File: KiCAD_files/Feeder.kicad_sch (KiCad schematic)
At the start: 82 parts, among them J405 Conn_01x02_Male, J406 Conn_01x02_Male, J501 Conn_01x03, Q501 60V N channel, Q502 TK13P25D,RQ, T501 PA2467NL, U407 OPA316, U501 NCP12700, U503 TL431MFDT,215

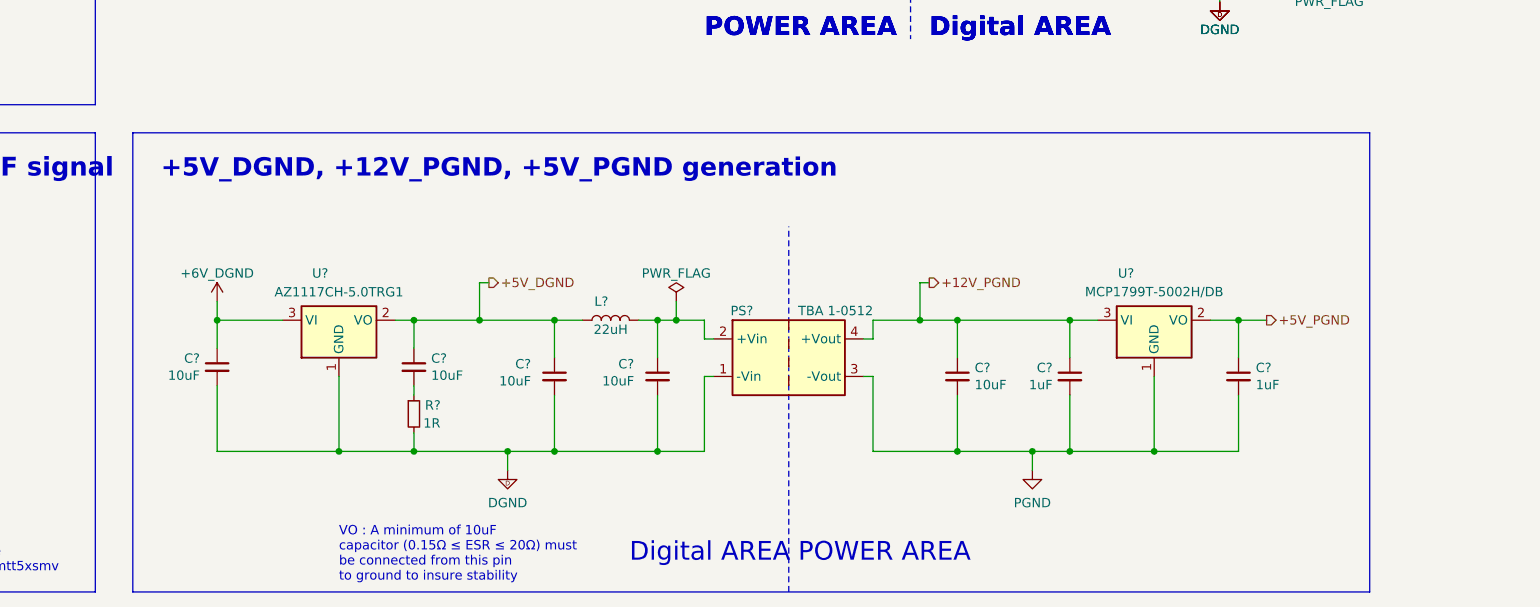
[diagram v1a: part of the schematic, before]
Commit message: added MCP1799T-5002H/DB in sch, forgot in previous commit
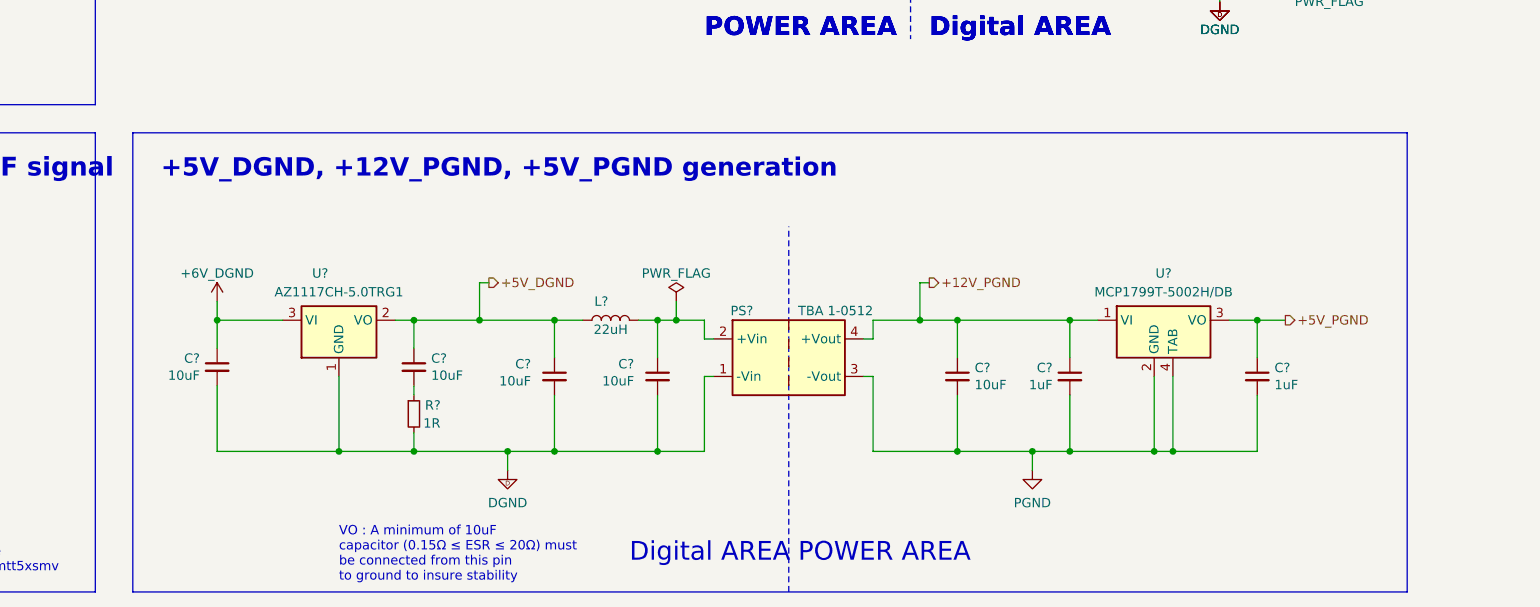
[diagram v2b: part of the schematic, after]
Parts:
- removed U?: MCP1799T-5002H/DB, Package_TO_SOT_SMD:SOT-223, symbol Regulator_Linear:MCP1754S-5002xCB
- added U?: MCP1799T-5002H/DB, Package_TO_SOT_SMD:SOT-223, symbol Symbols:MCP1799T-5002H/DB
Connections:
- net +12V_PGND: now also U?.1 (VI)
- net +5V_PGND: now also U?.3 (VO)
- net PGND: now also U?.2 (GND), U?.4 (TAB)
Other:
- moved on the sheet: C?
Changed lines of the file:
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@@
   (junction (at 154.94 127) (diameter 0) (color 0 0 0 0)
   )
-  (junction (at 264.16 261.62) (diameter 0) (color 0 0 0 0)
+  (junction (at 266.7 261.62) (diameter 0) (color 0 0 0 0)
   )
   (junction (at 49.53 96.52) (diameter 0) (color 0 0 0 0)
@@
   (junction (at 247.65 261.62) (diameter 0) (color 0 0 0 0)
   )
+  (junction (at 264.16 261.62) (diameter 0) (color 0 0 0 0)
+  )
   (junction (at 182.88 261.62) (diameter 0) (color 0 0 0 0)
   )
@@
   (junction (at 153.67 261.62) (diameter 0) (color 0 0 0 0)
   )
-  (junction (at 275.59 243.84) (diameter 0) (color 0 0 0 0)
-  )
   (junction (at 196.85 243.84) (diameter 0) (color 0 0 0 0)
   )
@@
   (junction (at 181.61 104.14) (diameter 0) (color 0 0 0 0)
   )
+  (junction (at 278.13 243.84) (diameter 0) (color 0 0 0 0)
+  )
   (junction (at 285.75 185.42) (diameter 0) (color 0 0 0 0)
   )
@@
   (junction (at 273.05 176.53) (diameter 0) (color 0 0 0 0)
   )
+  (wire (pts (xy 266.7 261.62) (xy 278.13 261.62))
+    (stroke (width 0.5) (type default))
+  )
   (wire (pts (xy 38.1 261.62) (xy 38.1 267.97))
     (stroke (width 0) (type default))
@@
     (stroke (width 0.5) (type default))
   )
+  (wire (pts (xy 264.16 251.46) (xy 264.16 261.62))
+    (stroke (width 0.5) (type default))
+  )
   (wire (pts (xy 64.77 187.96) (xy 64.77 189.23))
     (stroke (width 0) (type default))
@@
     (stroke (width 0) (type default))
   )
-  (wire (pts (xy 271.78 243.84) (xy 275.59 243.84))
-    (stroke (width 0.5) (type default))
-  )
   (wire (pts (xy 165.1 147.32) (xy 165.1 153.67))
     (stroke (width 0) (type default))
@@
     (stroke (width 0) (type default))
   )
-  (wire (pts (xy 275.59 254) (xy 275.59 261.62))
+  (wire (pts (xy 278.13 254) (xy 278.13 261.62))
     (stroke (width 0.5) (type default))
   )
@@
     (stroke (width 0.5) (type default))
   )
-  (wire (pts (xy 275.59 248.92) (xy 275.59 243.84))
+  (wire (pts (xy 278.13 248.92) (xy 278.13 243.84))
     (stroke (width 0.5) (type default))
   )
@@
     (stroke (width 0) (type default))
   )
+  (wire (pts (xy 266.7 251.46) (xy 266.7 261.62))
+    (stroke (width 0.5) (type default))
+  )
   (wire (pts (xy 205.74 104.14) (xy 219.71 104.14))
     (stroke (width 0) (type default))
   )
-  (wire (pts (xy 264.16 251.46) (xy 264.16 261.62))
-    (stroke (width 0.5) (type default))
-  )
   (wire (pts (xy 327.66 106.68) (xy 327.66 109.22))
     (stroke (width 0.5) (type default))
@@
     (stroke (width 0) (type default))
   )
-  (wire (pts (xy 275.59 261.62) (xy 264.16 261.62))
-    (stroke (width 0.5) (type default))
-  )
   (wire (pts (xy 247.65 261.62) (xy 252.73 261.62))
     (stroke (width 0.5) (type default))
@@
     (stroke (width 0.5) (type default))
   )
+  (wire (pts (xy 274.32 243.84) (xy 278.13 243.84))
+    (stroke (width 0.5) (type default))
+  )
   (wire (pts (xy 181.61 104.14) (xy 181.61 101.6))
     (stroke (width 0) (type default))
@@
     (stroke (width 0.5) (type default))
   )
-  (wire (pts (xy 275.59 243.84) (xy 279.4 243.84))
+  (wire (pts (xy 278.13 243.84) (xy 281.94 243.84))
     (stroke (width 0.5) (type default))
   )
@@
     (stroke (width 0) (type default))
   )
+  (wire (pts (xy 264.16 261.62) (xy 266.7 261.62))
+    (stroke (width 0.5) (type default))
+  )
   (wire (pts (xy 285.75 90.17) (xy 285.75 118.11))
     (stroke (width 0) (type default))
@@
     (fill (type none))
   )
-  (rectangle (start 125.73 218.44) (end 293.37 280.67)
+  (rectangle (start 125.73 218.44) (end 298.45 280.67)
     (stroke (width 0) (type default))
     (fill (type none))
@@
     (effects (font (size 1.27 1.27)) (justify left))
   )
-  (hierarchical_label "+5V_PGND" (shape output) (at 279.4 243.84 0) (fields_autoplaced)
+  (hierarchical_label "+5V_PGND" (shape output) (at 281.94 243.84 0) (fields_autoplaced)
     (effects (font (size 1.27 1.27)) (justify left))
   )
@@
     )
   )
+  (symbol (lib_id "Symbols:MCP1799T-5002H/DB") (at 264.16 243.84 0) (unit 1)
+    (in_bom yes) (on_board yes) (dnp no) (fields_autoplaced)
+    (property "Reference" "U?" (at 265.43 237.49 0)
+      (effects (font (size 1.27 1.27)))
+    )
+    (property "Value" "MCP1799T-5002H/DB" (at 265.43 240.03 0)
+      (effects (font (size 1.27 1.27)))
+    )
+    (property "Footprint" "Package_TO_SOT_SMD:SOT-223" (at 264.16 238.125 0)
+      (effects (font (size 1.27 1.27)) hide)
+    )
+    (property "Datasheet" "https://www.mouser.fr/datasheet/2/268/MCP1799_Data_Sheet_20006248B-2887414.pdf" (at 265.43 232.41 0)
+      (effects (font (size 1.27 1.27)) hide)
+    )
+    (property "manf#" "MCP1799T-5002H/DB" (at 264.16 243.84 0)
+      (effects (font (size 1.27 1.27)) hide)
+    )
+    (pin "1")
+    (pin "2")
+    (pin "3")
+    (pin "4")
+    (instances
+      (project "ownverter"
+        (path "/8d0c1d66-35ef-4a53-a28f-436a11b54f42/bce1534c-362e-45ed-a9dd-a44d6954485a"
+          (reference "U?") (unit 1)
+        )
+      )
+    )
+  )
   (symbol (lib_id "Device:R_Small") (at 38.1 259.08 180) (unit 1)
     (in_bom yes) (on_board yes) (dnp no)
@@
     )
   )
-  (symbol (lib_id "Regulator_Linear:MCP1754S-5002xCB") (at 264.16 243.84 0) (unit 1)
-    (in_bom yes) (on_board yes) (dnp no)
-    (property "Reference" "U?" (at 260.35 237.49 0)
-      (effects (font (size 1.27 1.27)))
-    )
-    (property "Value" "MCP1799T-5002H/DB" (at 264.16 240.0046 0)
-      (effects (font (size 1.27 1.27)))
-    )
-    (property "Footprint" "Package_TO_SOT_SMD:SOT-223" (at 264.16 238.125 0)
-      (effects (font (size 1.27 1.27)) hide)
-    )
-    (property "Datasheet" "https://www.mouser.fr/datasheet/2/268/MCP1799_Data_Sheet_20006248B-2887414.pdf" (at 264.16 243.84 0)
-      (effects (font (size 1.27 1.27)) hide)
-    )
-    (property "DNP" "x" (at 264.16 243.84 0)
-      (effects (font (size 1.27 1.27)) hide)
-    )
-    (property "manf#" "MCP1799T-5002H/DB" (at 264.16 243.84 0)
-      (effects (font (size 1.27 1.27)) hide)
-    )
-    (pin "1")
-    (pin "2")
-    (pin "3")
-    (instances
-      (project "ownverter"
-        (path "/8d0c1d66-35ef-4a53-a28f-436a11b54f42/122c01f4-f23e-4db0-9503-7261d96dc78b"
-          (reference "U?") (unit 1)
-        )
-        (path "/8d0c1d66-35ef-4a53-a28f-436a11b54f42"
-          (reference "U?") (unit 1)
-        )
-        (path "/8d0c1d66-35ef-4a53-a28f-436a11b54f42/bce1534c-362e-45ed-a9dd-a44d6954485a"
-          (reference "U505") (unit 1)
-        )
-      )
-    )
-  )
   (symbol (lib_id "Device:L") (at 43.18 46.99 90) (unit 1)
     (in_bom yes) (on_board yes) (dnp no) (fields_autoplaced)
@@
     )
   )
-  (symbol (lib_id "Device:C_Small") (at 275.59 251.46 0) (unit 1)
+  (symbol (lib_id "Device:C_Small") (at 278.13 251.46 0) (unit 1)
     (in_bom yes) (on_board yes) (dnp no)
-    (property "Reference" "C?" (at 277.9268 250.2916 0)
+    (property "Reference" "C?" (at 280.4668 250.2916 0)
       (effects (font (size 1.27 1.27)) (justify left))
     )
-    (property "Value" "1uF" (at 277.9268 252.603 0)
+    (property "Value" "1uF" (at 280.4668 252.603 0)
       (effects (font (size 1.27 1.27)) (justify left))
     )
-    (property "Footprint" "Footprints:C_0805_2012Metric" (at 275.59 251.46 0)
+    (property "Footprint" "Footprints:C_0805_2012Metric" (at 278.13 251.46 0)
       (effects (font (size 1.27 1.27)) hide)
     )
-    (property "Datasheet" "~" (at 275.59 251.46 0)
+    (property "Datasheet" "~" (at 278.13 251.46 0)
       (effects (font (size 1.27 1.27)) hide)
     )
-    (property "DNP" "x" (at 275.59 251.46 0)
+    (property "DNP" "x" (at 278.13 251.46 0)
       (effects (font (size 1.27 1.27)) hide)
     )
-    (property "manf#" "UMK212B7105KGHT " (at 275.59 251.46 0)
+    (property "manf#" "UMK212B7105KGHT " (at 278.13 251.46 0)
       (effects (font (size 1.27 1.27)) hide)
     )

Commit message: ready to import netlist
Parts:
- gave numbers to parts that had none: 1
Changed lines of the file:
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@@
   (symbol (lib_id "Symbols:MCP1799T-5002H/DB") (at 264.16 243.84 0) (unit 1)
     (in_bom yes) (on_board yes) (dnp no) (fields_autoplaced)
-    (property "Reference" "U?" (at 265.43 237.49 0)
+    (property "Reference" "U505" (at 265.43 237.49 0)
       (effects (font (size 1.27 1.27)))
     )
@@
       (project "ownverter"
         (path "/8d0c1d66-35ef-4a53-a28f-436a11b54f42/bce1534c-362e-45ed-a9dd-a44d6954485a"
-          (reference "U?") (unit 1)
+          (reference "U505") (unit 1)
         )
       )

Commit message: WIP PCB
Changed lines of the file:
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@@
     (stroke (width 0.5) (type default))
   )
-  (polyline (pts (xy 231.14 15.24) (xy 231.14 205.74))
+  (polyline (pts (xy 231.14 15.24) (xy 231.14 218.44))
     (stroke (width 0.15) (type dash))
   )

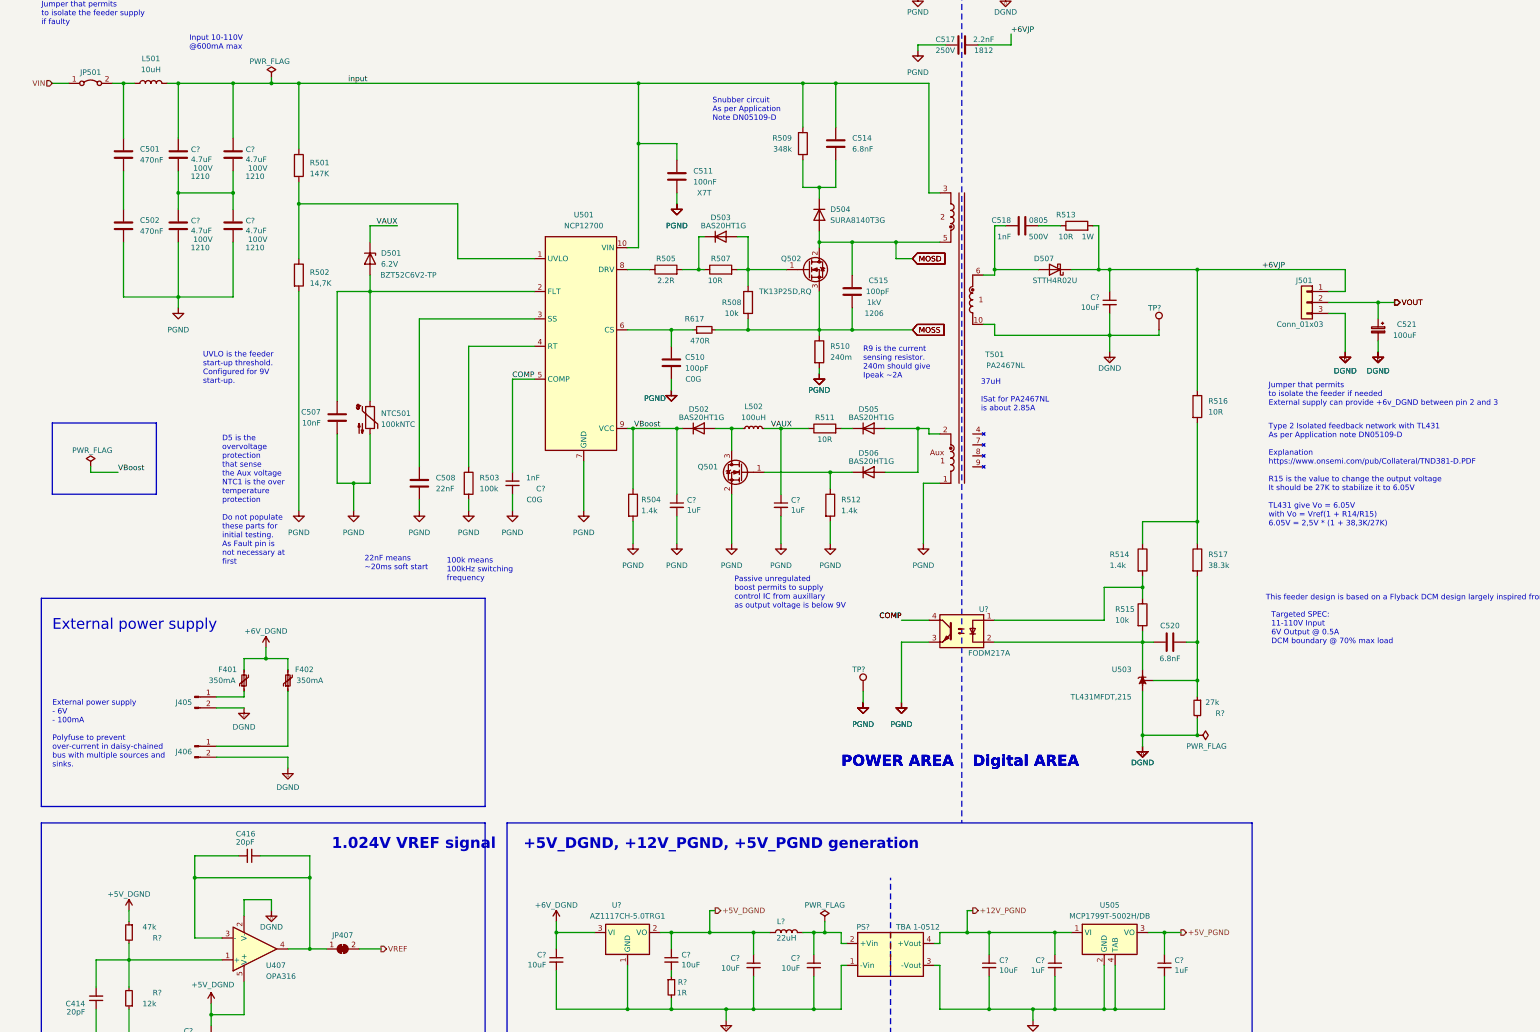
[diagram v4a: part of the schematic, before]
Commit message: changed schematic net labels for better comprehension
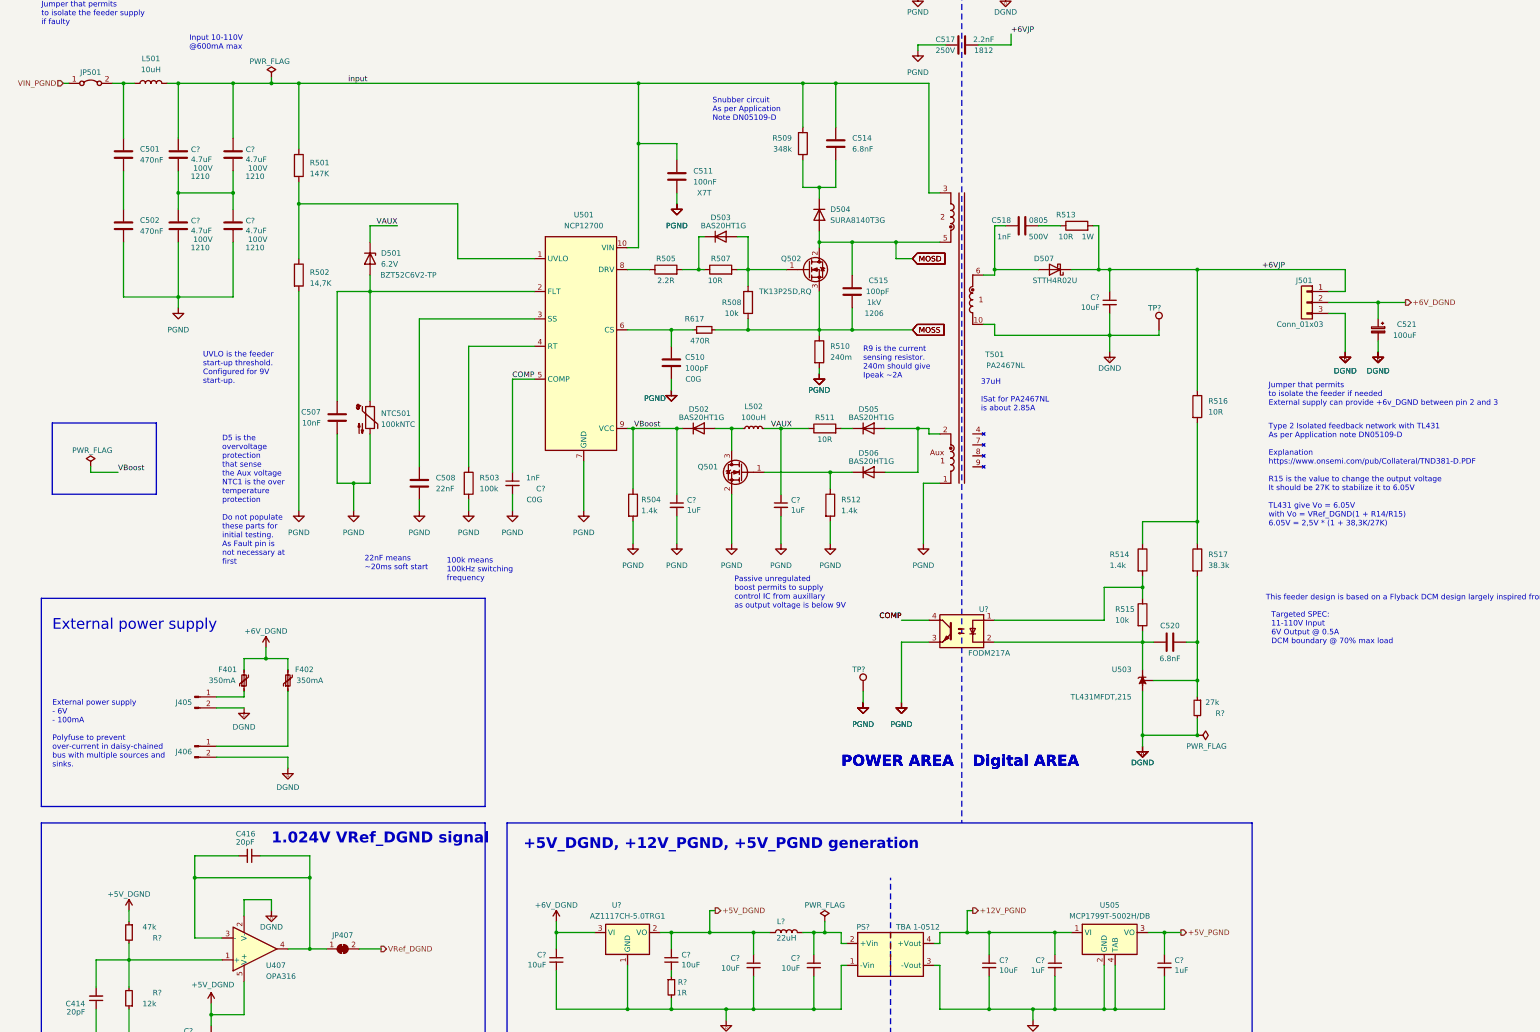
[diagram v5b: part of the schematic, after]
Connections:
- net VIN renamed VIN_PGND
- net VOUT renamed +6V_DGND
- net VREF renamed VRef_DGND
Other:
- note added: "1.024V VRef_DGND signal"
- note added: "Type 2 Isolated feedback network with TL431 As per Application note DN05109-D Explanation https://www.onsemi.com/pub/Collateral/TND381-D.PDF R15 is the value to change the output voltage It should be 27K to stabilize it to 6.05V TL431 give Vo = 6.05V with Vo = VRef_DGND(1 + R14/R15) 6.05V = 2,5V * (1 + 38,3K/27K)"
- note removed: "1.024V VREF signal"
- note removed: "Type 2 Isolated feedback network with TL431 As per Application note DN05109-D Explanation https://www.onsemi.com/pub/Collateral/TND381-D.PDF R15 is the value to change the output voltage It should be 27K to stabilize it to 6.05V TL431 give Vo = 6.05V with Vo = Vref(1 + R14/R15) 6.05V = 2,5V * (1 + 38,3K/27K)"
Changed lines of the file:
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@@
     (stroke (width 0) (type default))
   )
-  (wire (pts (xy 20.32 46.99) (xy 24.13 46.99))
+  (wire (pts (xy 22.86 46.99) (xy 24.13 46.99))
     (stroke (width 0.45) (type default))
   )
@@
     (stroke (width 0) (type default))
   )
-  (wire (pts (xy 331.47 97.79) (xy 327.66 97.79))
+  (wire (pts (xy 334.01 97.79) (xy 327.66 97.79))
     (stroke (width 0.5) (type default))
   )
@@
     (effects (font (size 2.54 2.54) (thickness 0.508) bold) (justify left bottom))
   )
-  (text "1.024V VREF signal" (at 85.09 224.79 0)
+  (text "1.024V VRef_DGND signal" (at 71.12 223.52 0)
     (effects (font (size 2.54 2.54) (thickness 0.508) bold) (justify left bottom))
   )
@@
     (effects (font (face "Arial") (size 2.4892 2.4892) (thickness 0.4978) bold) (justify left bottom))
   )
-  (text "Type 2 Isolated feedback network with TL431\nAs per Application note DN05109-D\n\nExplanation\nhttps://www.onsemi.com/pub/Collateral/TND381-D.PDF\n\nR15 is the value to change the output voltage\nIt should be 27K to stabilize it to 6.05V\n\nTL431 give Vo = 6.05V\nwith Vo = Vref(1 + R14/R15)\n6.05V = 2,5V * (1 + 38,3K/27K)"
+  (text "Type 2 Isolated feedback network with TL431\nAs per Application note DN05109-D\n\nExplanation\nhttps://www.onsemi.com/pub/Collateral/TND381-D.PDF\n\nR15 is the value to change the output voltage\nIt should be 27K to stabilize it to 6.05V\n\nTL431 give Vo = 6.05V\nwith Vo = VRef_DGND(1 + R14/R15)\n6.05V = 2,5V * (1 + 38,3K/27K)"
     (at 302.26 149.86 0)
     (effects (font (size 1.27 1.27)) (justify left bottom))
@@
     )
   )
-  (hierarchical_label "VIN" (shape input) (at 20.32 46.99 180) (fields_autoplaced)
+  (hierarchical_label "VIN_PGND" (shape input) (at 22.86 46.99 180) (fields_autoplaced)
     (effects (font (size 1.27 1.27)) (justify right))
   )
-  (hierarchical_label "VOUT" (shape output) (at 331.47 97.79 0) (fields_autoplaced)
-    (effects (font (size 1.27 1.27)) (justify left))
-  )
-  (hierarchical_label "VOUT" (shape output) (at 331.47 97.79 0) (fields_autoplaced)
+  (hierarchical_label "+6V_DGND" (shape output) (at 334.01 97.79 0) (fields_autoplaced)
     (effects (font (size 1.27 1.27)) (justify left))
   )
@@
     (effects (font (size 1.27 1.27)) (justify left))
   )
-  (hierarchical_label "VREF" (shape output) (at 96.52 247.65 0) (fields_autoplaced)
+  (hierarchical_label "VRef_DGND" (shape output) (at 96.52 247.65 0) (fields_autoplaced)
     (effects (font (size 1.27 1.27)) (justify left))
   )
